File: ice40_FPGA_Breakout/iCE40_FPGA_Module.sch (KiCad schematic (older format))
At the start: 0 parts

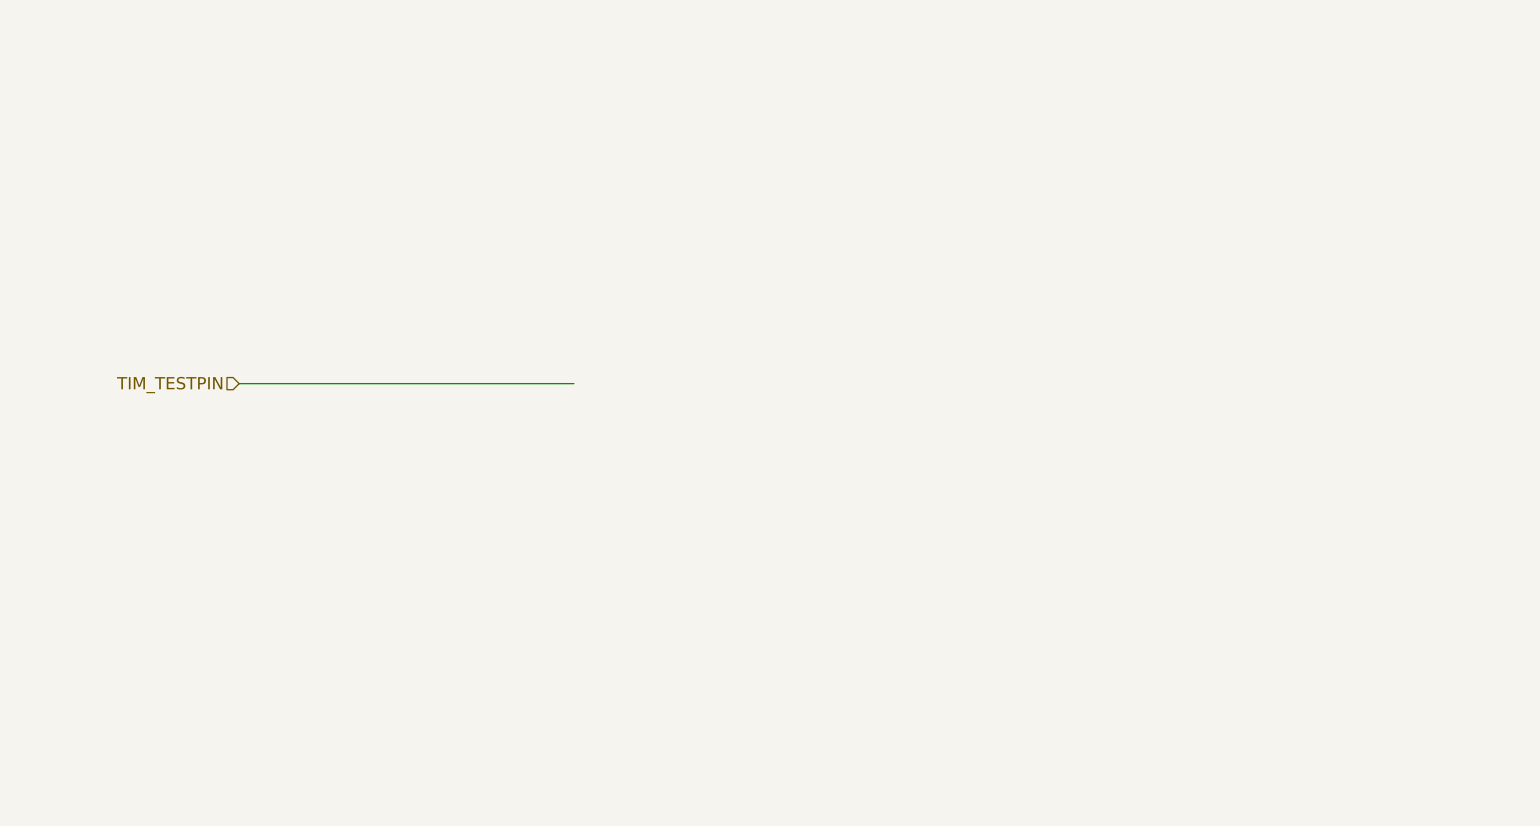
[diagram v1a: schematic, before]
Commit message: FTDI, iCE40 chip differential pair schematic
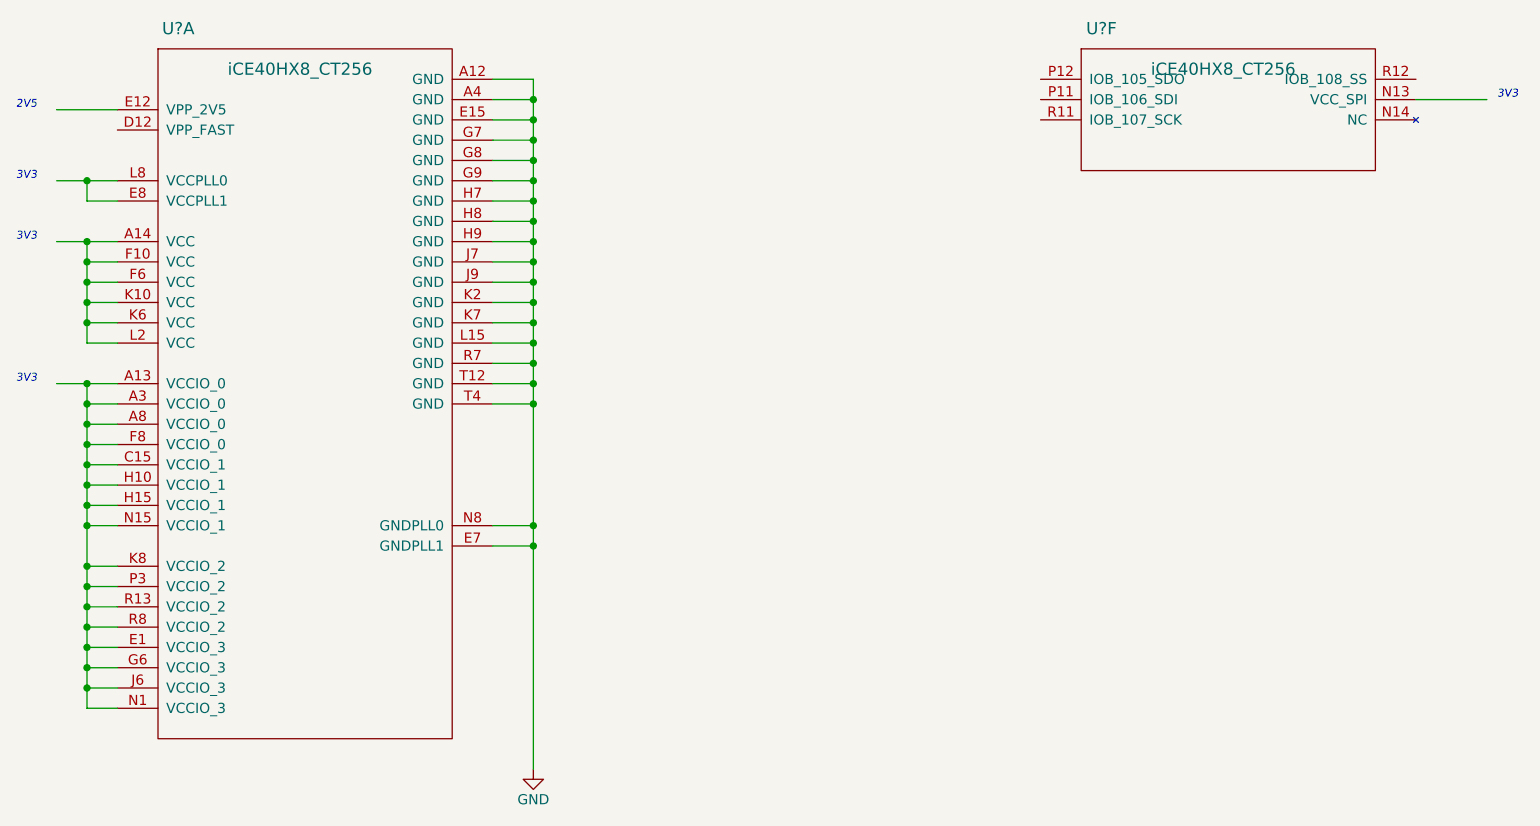
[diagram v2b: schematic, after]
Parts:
- added U? (x2): iCE40HX8_CT256, symbol iCE40HX8_CT256
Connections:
- net labels added: GND
- net labels removed: TIM_TESTPIN
- wire segments 1 -> 49
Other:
- note added: "2V5"
- note added: "3V3"
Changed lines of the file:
@@
 LIBS:zetex
 LIBS:Zilog
+LIBS:gti_Lattice
 LIBS:ice40-hx8K_breakout_brd-cache
 EELAYER 25 0
@@
 Comment4 ""
 $EndDescr
-Text HLabel 3400 3250 0    60   Input ~ 0
-TIM_TESTPIN
+$Comp
+L iCE40HX8_CT256 U?
+U 1 1 5A2426BF
+P 3000 1600
+F 0 "U?" H 3100 1700 60  0000 C CNN
+F 1 "iCE40HX8_CT256" H 3700 1500 60  0000 C CNN
+F 2 "" H 3000 1600 60  0001 C CNN
+F 3 "" H 3000 1600 60  0001 C CNN
+	1    3000 1600
+	1    0    0    -1
+$EndComp
 Wire Wire Line
-	3400 3250 5050 3250
+	4650 1750 4850 1750
+Wire Wire Line
+	4850 1750 4850 5150
+Wire Wire Line
+	4650 4050 4850 4050
+Connection ~ 4850 4050
+Wire Wire Line
+	4650 3950 4850 3950
+Connection ~ 4850 3950
+Wire Wire Line
+	4650 3350 4850 3350
+Connection ~ 4850 3350
+Wire Wire Line
+	4650 3250 4850 3250
+Connection ~ 4850 3250
+Wire Wire Line
+	4650 3150 4850 3150
+Connection ~ 4850 3150
+Wire Wire Line
+	4650 3050 4850 3050
+Connection ~ 4850 3050
+Wire Wire Line
+	4650 2950 4850 2950
+Connection ~ 4850 2950
+Wire Wire Line
+	4650 2850 4850 2850
+Connection ~ 4850 2850
+Wire Wire Line
+	4650 1850 4850 1850
+Connection ~ 4850 1850
+Wire Wire Line
+	4650 1950 4850 1950
+Connection ~ 4850 1950
+Wire Wire Line
+	4650 2050 4850 2050
+Connection ~ 4850 2050
+Wire Wire Line
+	4650 2150 4850 2150
+Connection ~ 4850 2150
+Wire Wire Line
+	4650 2250 4850 2250
+Connection ~ 4850 2250
+Wire Wire Line
+	4650 2350 4850 2350
+Connection ~ 4850 2350
+Wire Wire Line
+	4650 2450 4850 2450
+Connection ~ 4850 2450
+Wire Wire Line
+	4650 2550 4850 2550
+Connection ~ 4850 2550
+Wire Wire Line
+	4650 2650 4850 2650
+Connection ~ 4850 2650
+Wire Wire Line
+	4650 2750 4850 2750
+Connection ~ 4850 2750
+Wire Wire Line
+	2500 1900 2800 1900
+Wire Wire Line
+	2650 3050 2800 3050
+Wire Wire Line
+	2650 2550 2650 3050
+Wire Wire Line
+	2500 2550 2800 2550
+Connection ~ 2650 2550
+Wire Wire Line
+	2800 2650 2650 2650
+Connection ~ 2650 2650
+Wire Wire Line
+	2800 2750 2650 2750
+Connection ~ 2650 2750
+Wire Wire Line
+	2800 2850 2650 2850
+Connection ~ 2650 2850
+Wire Wire Line
+	2800 2950 2650 2950
+Connection ~ 2650 2950
+Wire Wire Line
+	2800 2350 2650 2350
+Wire Wire Line
+	2650 2350 2650 2250
+Wire Wire Line
+	2500 2250 2800 2250
+Connection ~ 2650 2250
+Wire Wire Line
+	2800 3550 2650 3550
+Wire Wire Line
+	2650 3250 2650 4850
+Wire Wire Line
+	2500 3250 2800 3250
+Connection ~ 2650 3250
+Wire Wire Line
+	2800 3350 2650 3350
+Connection ~ 2650 3350
+Wire Wire Line
+	2800 3450 2650 3450
+Connection ~ 2650 3450
+Wire Wire Line
+	2650 3950 2800 3950
+Connection ~ 2650 3550
+Wire Wire Line
+	2800 3850 2650 3850
+Connection ~ 2650 3850
+Wire Wire Line
+	2800 3750 2650 3750
+Connection ~ 2650 3750
+Wire Wire Line
+	2650 3650 2800 3650
+Connection ~ 2650 3650
+Wire Wire Line
+	2650 4850 2800 4850
+Connection ~ 2650 3950
+Wire Wire Line
+	2800 4150 2650 4150
+Connection ~ 2650 4150
+Wire Wire Line
+	2800 4250 2650 4250
+Connection ~ 2650 4250
+Wire Wire Line
+	2800 4350 2650 4350
+Connection ~ 2650 4350
+Wire Wire Line
+	2800 4450 2650 4450
+Connection ~ 2650 4450
+Wire Wire Line
+	2800 4550 2650 4550
+Connection ~ 2650 4550
+Wire Wire Line
+	2800 4650 2650 4650
+Connection ~ 2650 4650
+Wire Wire Line
+	2800 4750 2650 4750
+Connection ~ 2650 4750
+$Comp
+L GND #PWR01
+U 1 1 5A263712
+P 4850 5150
+F 0 "#PWR01" H 4850 4900 50  0001 C CNN
+F 1 "GND" H 4850 5000 50  0000 C CNN
+F 2 "" H 4850 5150 50  0001 C CNN
+F 3 "" H 4850 5150 50  0001 C CNN
+	1    4850 5150
+	1    0    0    -1
+$EndComp
+$Comp
+L iCE40HX8_CT256 U?
+U 6 1 5A264275
+P 7550 1600
+F 0 "U?" H 7650 1700 60  0000 C CNN
+F 1 "iCE40HX8_CT256" H 8250 1500 60  0000 C CNN
+F 2 "" H 7550 1600 60  0001 C CNN
+F 3 "" H 7550 1600 60  0001 C CNN
+	6    7550 1600
+	1    0    0    -1
+$EndComp
+Wire Wire Line
+	9200 1850 9550 1850
+Text Notes 2300 1900 0    39   Italic 0
+2V5
+Text Notes 2300 2250 0    39   Italic 0
+3V3
+Text Notes 2300 2550 0    39   Italic 0
+3V3
+Text Notes 2300 3250 0    39   Italic 0
+3V3
+Text Notes 9600 1850 0    39   Italic 0
+3V3
 $EndSCHEMATC

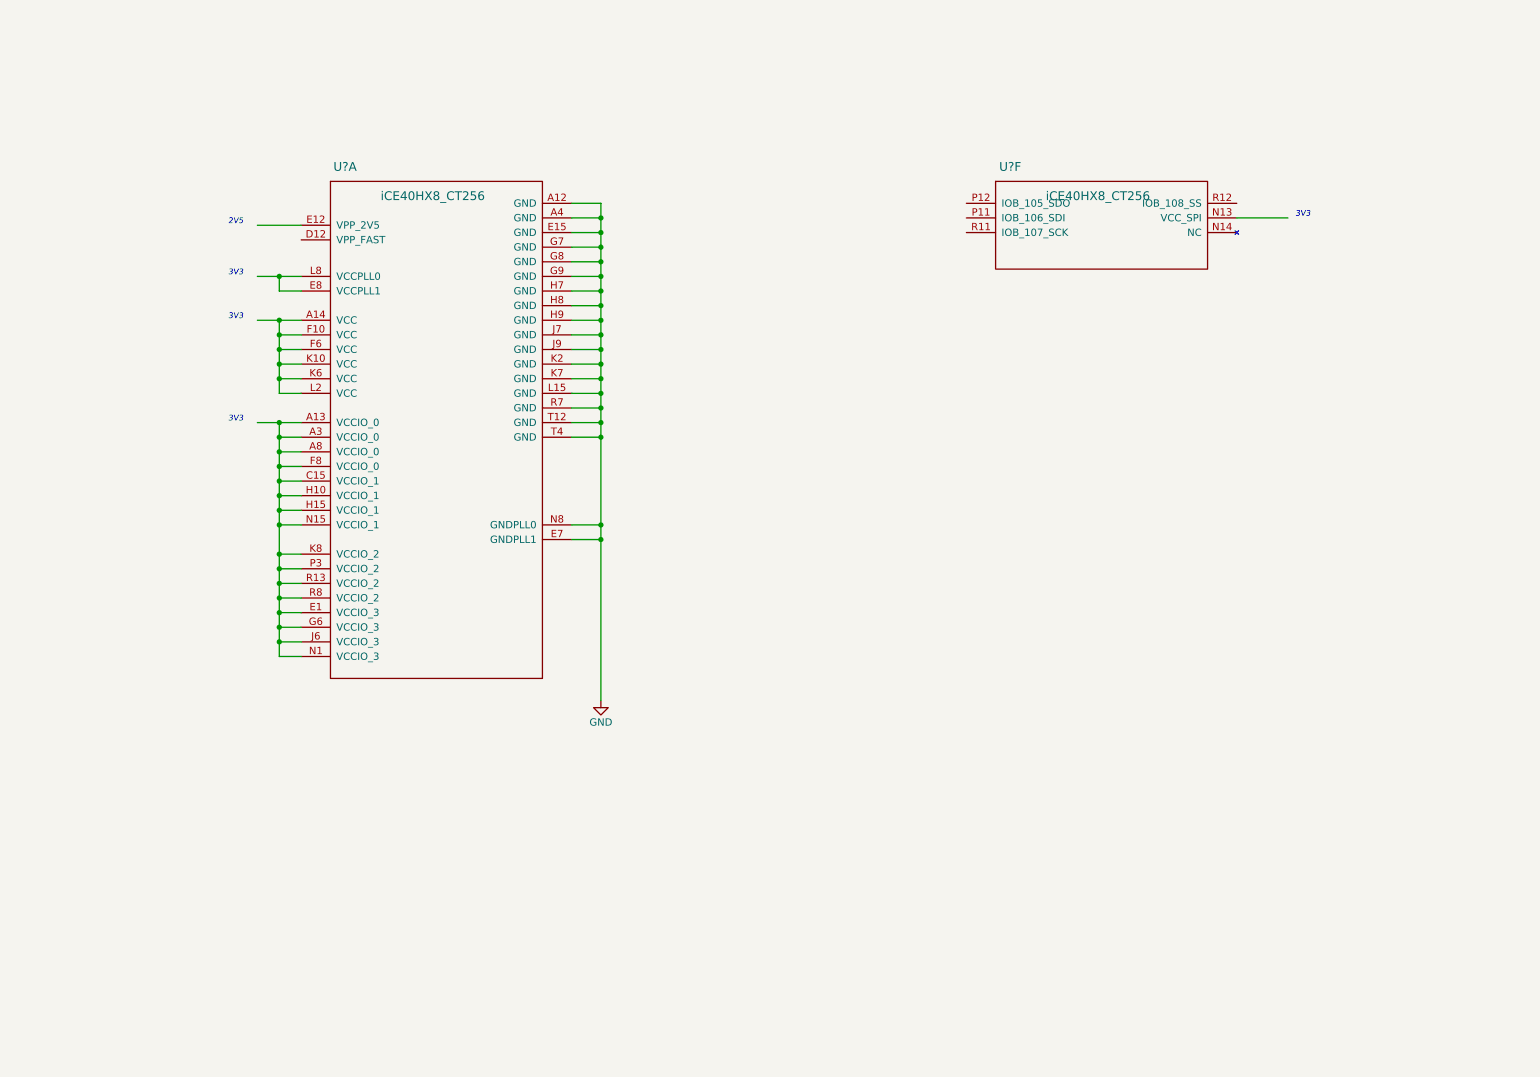
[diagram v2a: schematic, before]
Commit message: Added SO-DIMM header, ice40 IO and FTDI power
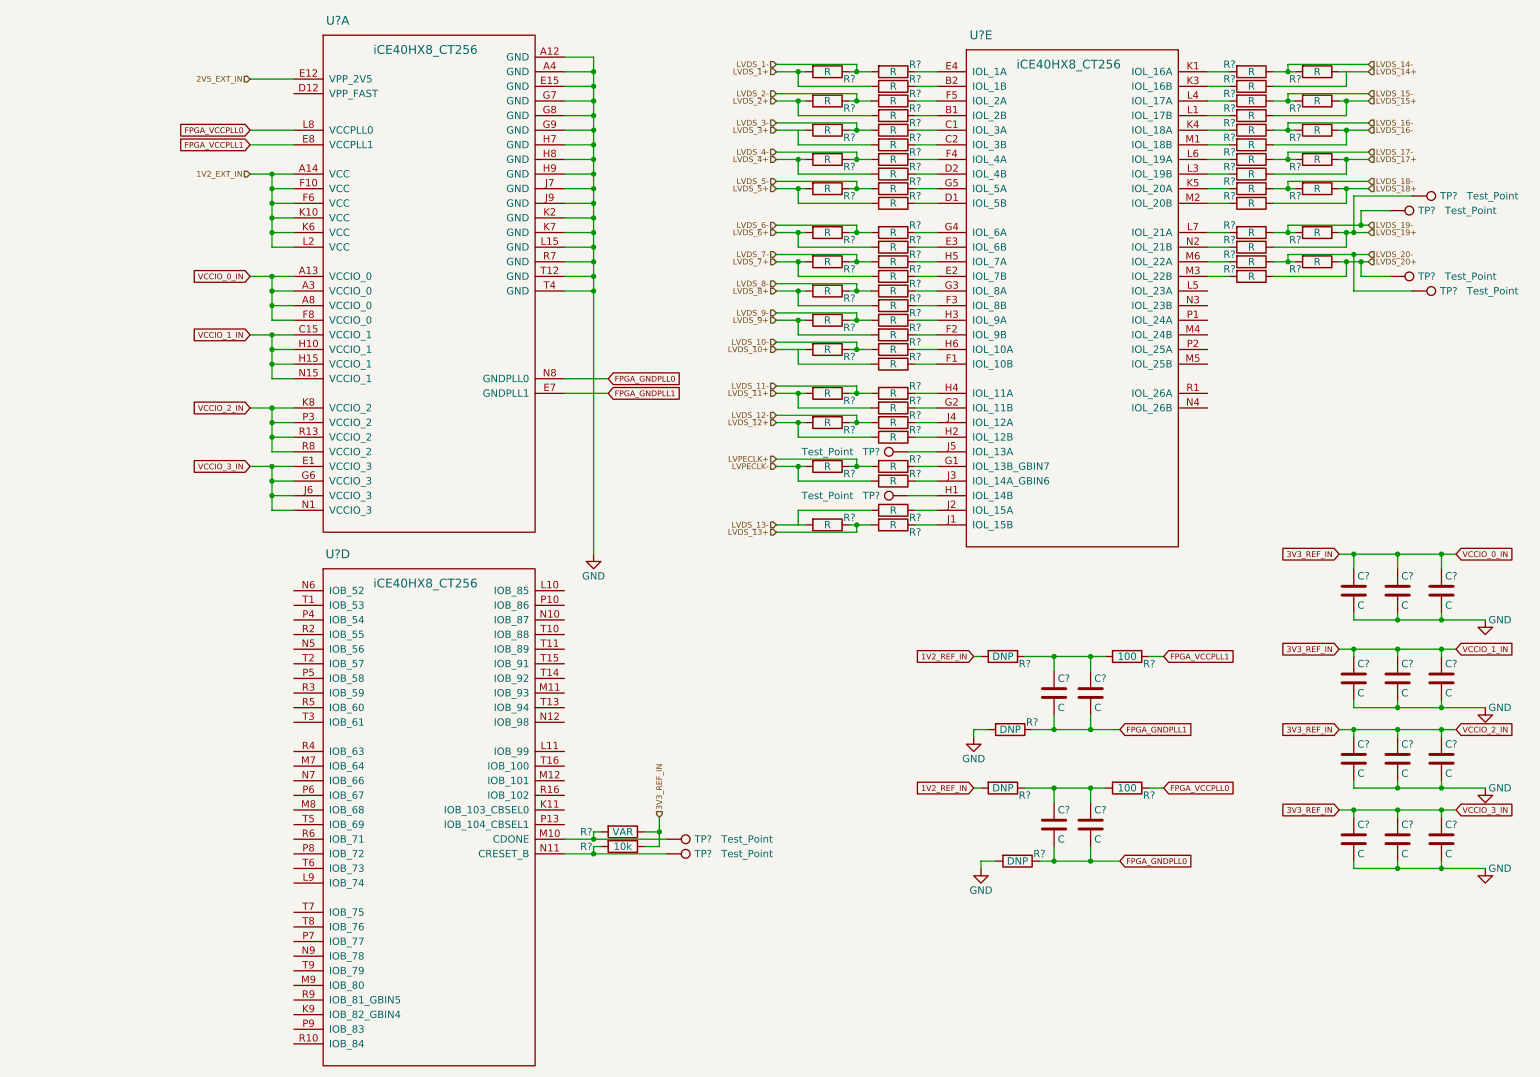
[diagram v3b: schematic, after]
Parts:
- removed U?: iCE40HX8_CT256, symbol iCE40HX8_CT256
- added C? (x16): C, symbol C
- added R? (x63): R, symbol R
- added R? (x4): DNP, symbol R
- added R?: 10k, symbol R
- added R?: VAR, symbol R
- added R? (x2): 100, symbol R
- added TP? (x8): Test_Point, symbol Test_Point
- added U? (x2): iCE40HX8_CT256, symbol iCE40HX8_CT256
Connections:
- net labels added: 1V2_EXT_IN, 1V2_REF_IN, 2V5_EXT_IN, 3V3_REF_IN, FPGA_GNDPLL0, FPGA_GNDPLL1, FPGA_VCCPLL0, FPGA_VCCPLL1, LVDS_1+, LVDS_1-, LVDS_10+, LVDS_10-, LVDS_11+, LVDS_11-, LVDS_12+, LVDS_12-, LVDS_13+, LVDS_13-, LVDS_14+, LVDS_14-, LVDS_15+, LVDS_15-, LVDS_16-, LVDS_17+, LVDS_17-, LVDS_18+, LVDS_18-, LVDS_19+, LVDS_19-, LVDS_2+, LVDS_2-, LVDS_20+, LVDS_20-, LVDS_3+, LVDS_3-, LVDS_4+, LVDS_4-, LVDS_5+, LVDS_5-, LVDS_6+, LVDS_6-, LVDS_7+, LVDS_7-, LVDS_8+, LVDS_8-, LVDS_9+, LVDS_9-, LVPECLK+, LVPECLK-, VCCIO_0_IN, VCCIO_1_IN, VCCIO_2_IN, VCCIO_3_IN
- wire segments 49 -> 289
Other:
- note removed: "2V5"
- note removed: "3V3"
- moved on the sheet: U?A

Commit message: R/C value updated to FTDI section and also BD port UART logic added
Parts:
- C? (x6): value C -> 1uF
- C? (x6): value C -> 0.1uF
- C? (x4): value C -> 0.01uF
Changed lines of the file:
@@
 P 7950 6000
 F 0 "C?" H 7975 6100 50  0000 L CNN
-F 1 "C" H 7975 5900 50  0000 L CNN
+F 1 "1uF" H 7975 5900 50  0000 L CNN
 F 2 "" H 7988 5850 50  0001 C CNN
 F 3 "" H 7950 6000 50  0001 C CNN
@@
 P 8200 6000
 F 0 "C?" H 8225 6100 50  0000 L CNN
-F 1 "C" H 8225 5900 50  0000 L CNN
+F 1 "0.1uF" H 8225 5900 50  0000 L CNN
 F 2 "" H 8238 5850 50  0001 C CNN
 F 3 "" H 8200 6000 50  0001 C CNN
@@
 P 7950 5100
 F 0 "C?" H 7975 5200 50  0000 L CNN
-F 1 "C" H 7975 5000 50  0000 L CNN
+F 1 "1uF" H 7975 5000 50  0000 L CNN
 F 2 "" H 7988 4950 50  0001 C CNN
 F 3 "" H 7950 5100 50  0001 C CNN
@@
 P 8200 5100
 F 0 "C?" H 8225 5200 50  0000 L CNN
-F 1 "C" H 8225 5000 50  0000 L CNN
+F 1 "0.1uF" H 8225 5000 50  0000 L CNN
 F 2 "" H 8238 4950 50  0001 C CNN
 F 3 "" H 8200 5100 50  0001 C CNN
@@
 P 10000 4400
 F 0 "C?" H 10025 4500 50  0000 L CNN
-F 1 "C" H 10025 4300 50  0000 L CNN
+F 1 "1uF" H 10025 4300 50  0000 L CNN
 F 2 "" H 10038 4250 50  0001 C CNN
 F 3 "" H 10000 4400 50  0001 C CNN
@@
 P 10300 5000
 F 0 "C?" H 10325 5100 50  0000 L CNN
-F 1 "C" H 10325 4900 50  0000 L CNN
+F 1 "0.1uF" H 10325 4900 50  0000 L CNN
 F 2 "" H 10338 4850 50  0001 C CNN
 F 3 "" H 10300 5000 50  0001 C CNN
@@
 P 10600 5000
 F 0 "C?" H 10625 5100 50  0000 L CNN
-F 1 "C" H 10625 4900 50  0000 L CNN
+F 1 "0.01uF" H 10625 4900 50  0000 L CNN
 F 2 "" H 10638 4850 50  0001 C CNN
 F 3 "" H 10600 5000 50  0001 C CNN
@@
 P 10000 5550
 F 0 "C?" H 10025 5650 50  0000 L CNN
-F 1 "C" H 10025 5450 50  0000 L CNN
+F 1 "1uF" H 10025 5450 50  0000 L CNN
 F 2 "" H 10038 5400 50  0001 C CNN
 F 3 "" H 10000 5550 50  0001 C CNN
@@
 P 10300 5550
 F 0 "C?" H 10325 5650 50  0000 L CNN
-F 1 "C" H 10325 5450 50  0000 L CNN
+F 1 "0.1uF" H 10325 5450 50  0000 L CNN
 F 2 "" H 10338 5400 50  0001 C CNN
 F 3 "" H 10300 5550 50  0001 C CNN
@@
 P 10600 5550
 F 0 "C?" H 10625 5650 50  0000 L CNN
-F 1 "C" H 10625 5450 50  0000 L CNN
+F 1 "0.01uF" H 10625 5450 50  0000 L CNN
 F 2 "" H 10638 5400 50  0001 C CNN
 F 3 "" H 10600 5550 50  0001 C CNN
@@
 P 10000 6100
 F 0 "C?" H 10025 6200 50  0000 L CNN
-F 1 "C" H 10025 6000 50  0000 L CNN
+F 1 "1uF" H 10025 6000 50  0000 L CNN
 F 2 "" H 10038 5950 50  0001 C CNN
 F 3 "" H 10000 6100 50  0001 C CNN
@@
 P 10300 6100
 F 0 "C?" H 10325 6200 50  0000 L CNN
-F 1 "C" H 10325 6000 50  0000 L CNN
+F 1 "0.1uF" H 10325 6000 50  0000 L CNN
 F 2 "" H 10338 5950 50  0001 C CNN
 F 3 "" H 10300 6100 50  0001 C CNN
@@
 P 10600 6100
 F 0 "C?" H 10625 6200 50  0000 L CNN
-F 1 "C" H 10625 6000 50  0000 L CNN
+F 1 "0.01uF" H 10625 6000 50  0000 L CNN
 F 2 "" H 10638 5950 50  0001 C CNN
 F 3 "" H 10600 6100 50  0001 C CNN
@@
 P 10000 5000
 F 0 "C?" H 10025 5100 50  0000 L CNN
-F 1 "C" H 10025 4900 50  0000 L CNN
+F 1 "1uF" H 10025 4900 50  0000 L CNN
 F 2 "" H 10038 4850 50  0001 C CNN
 F 3 "" H 10000 5000 50  0001 C CNN
@@
 P 10300 4400
 F 0 "C?" H 10325 4500 50  0000 L CNN
-F 1 "C" H 10325 4300 50  0000 L CNN
+F 1 "0.1uF" H 10325 4300 50  0000 L CNN
 F 2 "" H 10338 4250 50  0001 C CNN
 F 3 "" H 10300 4400 50  0001 C CNN
@@
 P 10600 4400
 F 0 "C?" H 10625 4500 50  0000 L CNN
-F 1 "C" H 10625 4300 50  0000 L CNN
+F 1 "0.01uF" H 10625 4300 50  0000 L CNN
 F 2 "" H 10638 4250 50  0001 C CNN
 F 3 "" H 10600 4400 50  0001 C CNN

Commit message: Add SPI EEPROM logic for SPI switching
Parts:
- added C?: 0.01uF, symbol C
- added R? (x2): 10k, symbol R
- R? (x42): value R -> 253
- R? (x21): value R -> 50
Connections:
- net 3V3_REF_IN: no longer R?.1, R?.1
- net GND: now also C?.2
- net LVDS_1+ renamed LVDS_1_D+
- net LVDS_1- renamed LVDS_1_D-
- net LVDS_10+ renamed LVDS_10_D+
- net LVDS_10- renamed LVDS_10_D-
- net LVDS_11+ renamed LVDS_11_D+
- net LVDS_11- renamed LVDS_11_D-
- net LVDS_12+ renamed LVDS_12_D+
- net LVDS_12- renamed LVDS_12_D-
- net LVDS_13+ renamed LVDS_13_D+
- net LVDS_13- renamed LVDS_13_D-
- net LVDS_14+ renamed LVDS_14_D+
- net LVDS_14- renamed LVDS_14_D-
- net LVDS_15+ renamed LVDS_15_D+
- net LVDS_15- renamed LVDS_15_D-
- net LVDS_16- renamed LVDS_16_D+
- net LVDS_16_D+: no longer R?.1, R?.2
- net LVDS_17+ renamed LVDS_17_D+
- net LVDS_17- renamed LVDS_17_D-
- net LVDS_18+ renamed LVDS_18_D+
- net LVDS_18- renamed LVDS_18_D-
- net LVDS_19+ renamed LVDS_19_D+
- net LVDS_19- renamed LVDS_19_D-
- net LVDS_2+ renamed LVDS_2_D+
- net LVDS_2- renamed LVDS_2_D-
- net LVDS_20+ renamed LVDS_20_D+
- net LVDS_20- renamed LVDS_20_D-
- net LVDS_3+ renamed LVDS_3_D+
- net LVDS_3- renamed LVDS_3_D-
- net LVDS_4+ renamed LVDS_4_D+
- net LVDS_4- renamed LVDS_4_D-
- net LVDS_5+ renamed LVDS_5_D+
- net LVDS_5- renamed LVDS_5_D-
- net LVDS_6+ renamed LVDS_6_D+
- net LVDS_6- renamed LVDS_6_D-
- net LVDS_7+ renamed LVDS_7_D+
- net LVDS_7- renamed LVDS_7_D-
- net LVDS_8+ renamed LVDS_8_D+
- net LVDS_8- renamed LVDS_8_D-
- net LVDS_9+ renamed LVDS_9_D+
- net LVDS_9- renamed LVDS_9_D-
- new net: C?.1, R?.1, R?.2, U?.N11 (CRESET_B)
- new net: R?.1, R?.2, U?.M10 (CDONE)
- new net 3V3_EXT_IN: R?.2, R?.2
- new net EXT_RESET: R?.1, TP?.1
- new net FTDI_AD6_GPIO6: R?.1, TP?.1
- new net LVDS_16_D-: R?.1, R?.2
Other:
- moved on the sheet: R?, TP?
